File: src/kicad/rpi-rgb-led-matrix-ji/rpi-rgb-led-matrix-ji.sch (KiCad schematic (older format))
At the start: 41 parts, among them J1 Conn_01x02_Male, J2 Conn_02x10_Odd_Even, J3 Screw_Terminal_01x02, J4 Conn_02x08_Odd_Even, J5 Conn_02x08_Odd_Even, J6 Conn_02x08_Odd_Even, P1 Raspberry_Pi_2_3, Q1 DMG2305UX, Q2 DMMT5401, U1 74HCT245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

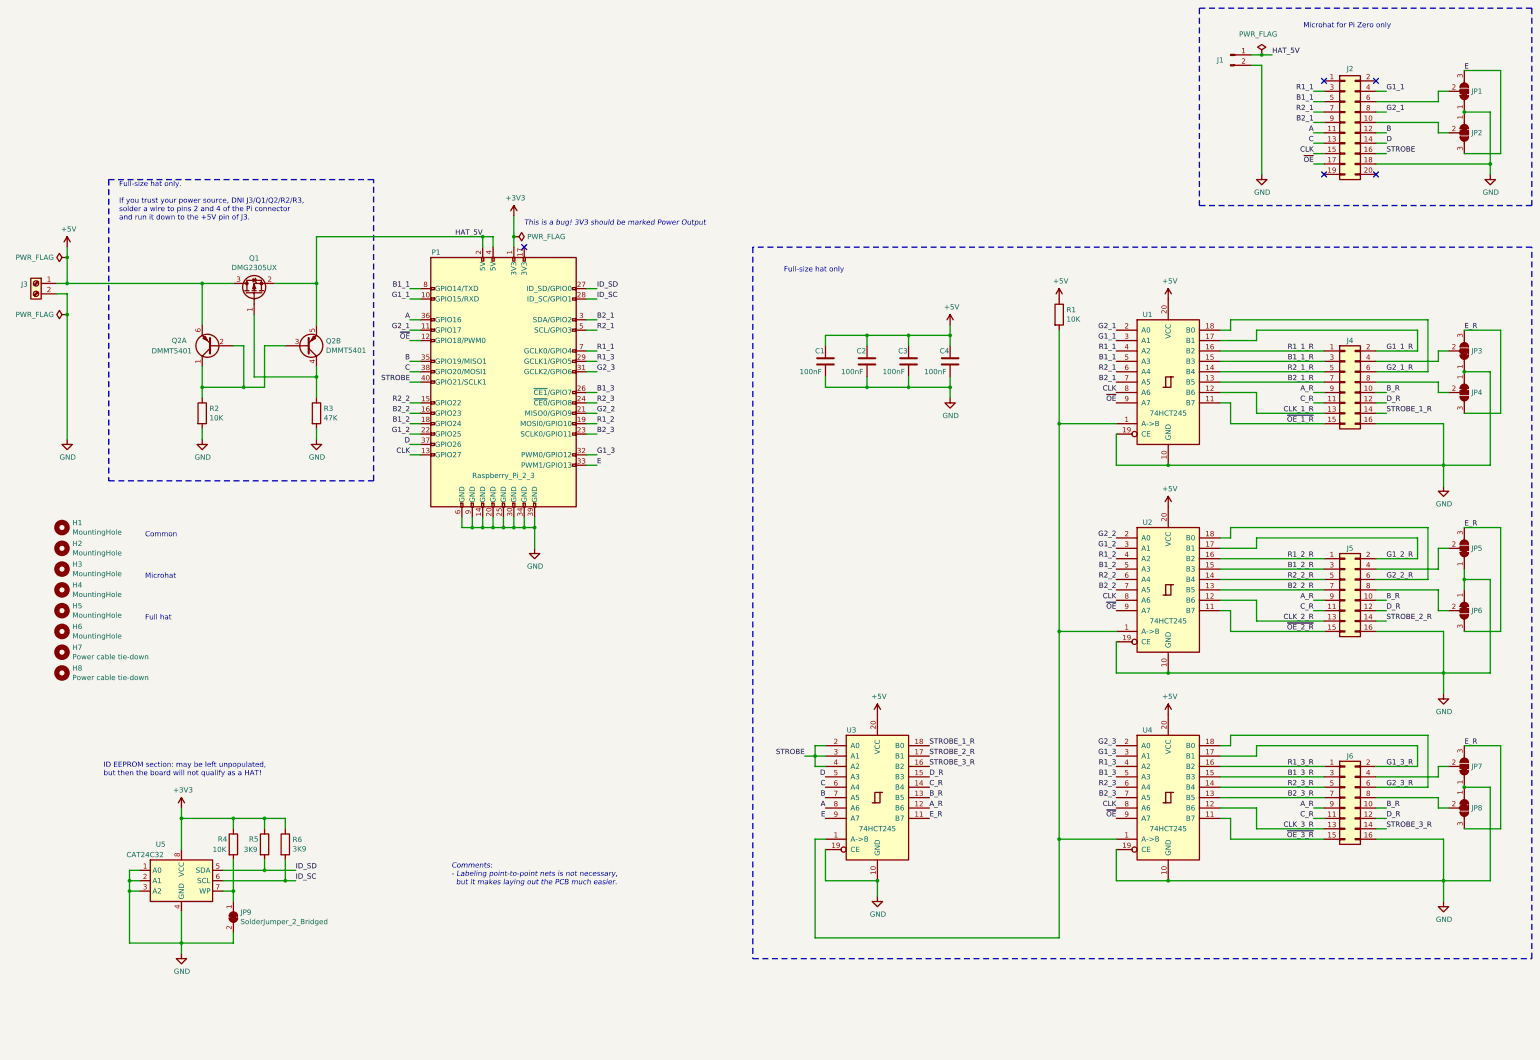
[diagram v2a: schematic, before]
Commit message: cleaned up PSU circuitry; added bypass capacitor to EEPROM
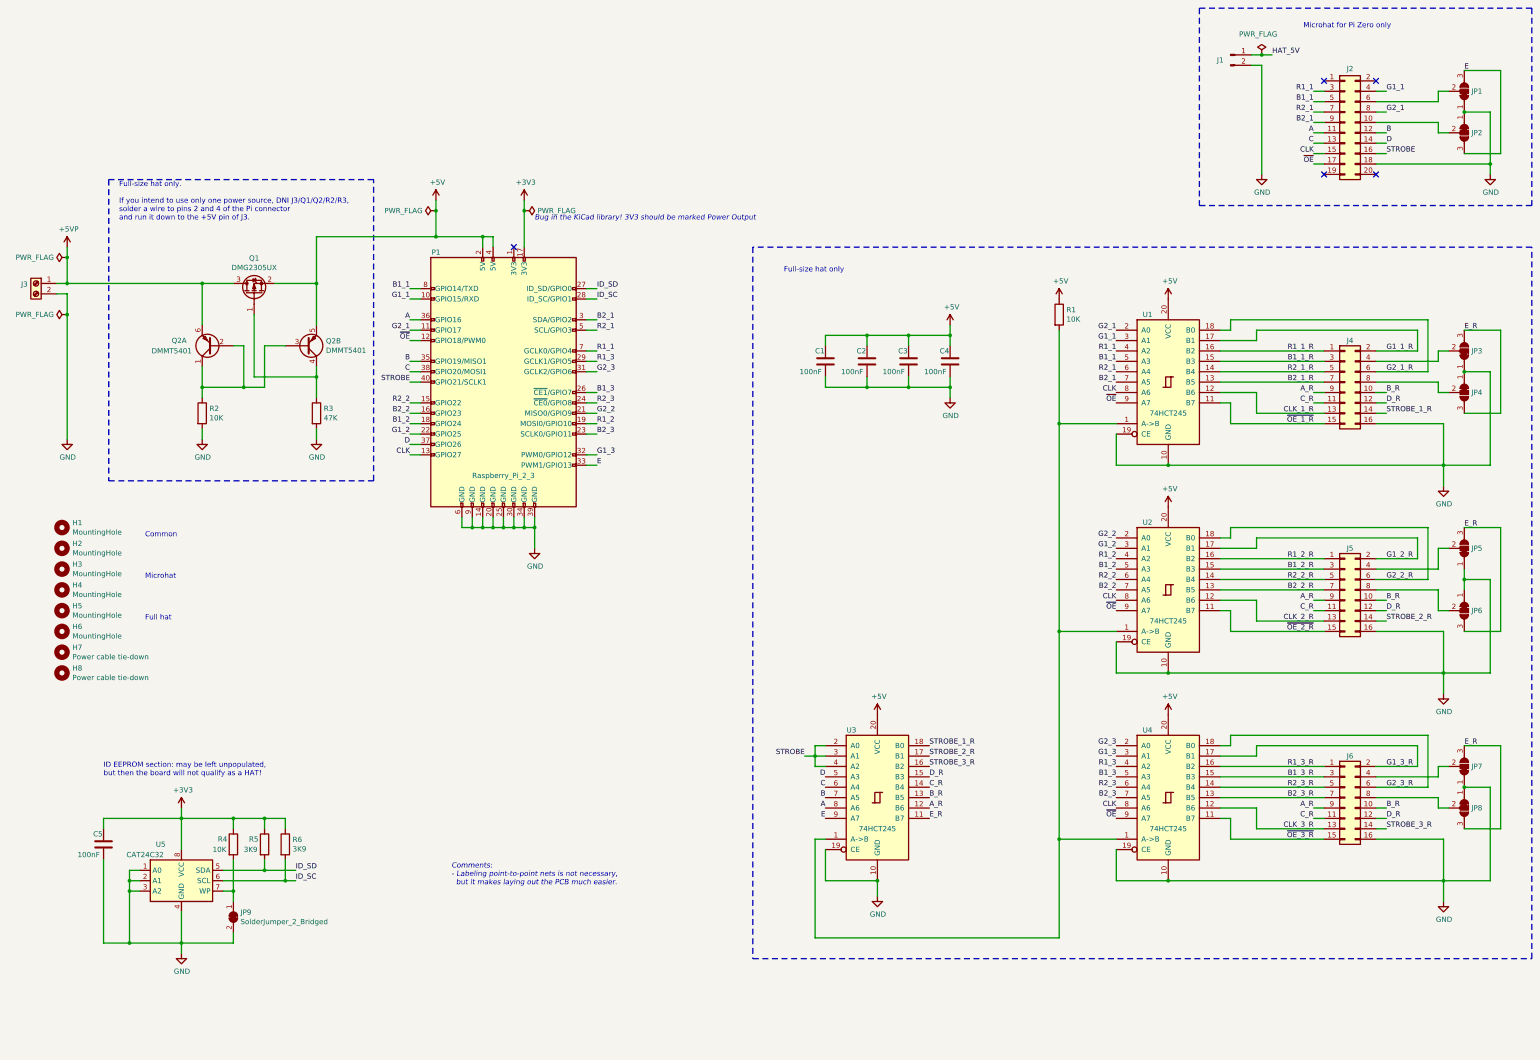
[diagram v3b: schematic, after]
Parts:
- added C5: 100nF, Capacitor_SMD:C_1206_3216Metric_Pad1.42x1.75mm_HandSolder, symbol Device:C
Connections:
- net +3V3: now also P1.17 (3V3), C5.1; no longer P1.1 (3V3)
- net +5V: now also P1.2 (5V), P1.4 (5V), Q1.2 (S), Q2.5 (E); no longer J3.1 (Pin_1), Q1.3 (D), Q2.6 (E)
- net GND: now also C5.2
- net HAT_5V: no longer P1.2 (5V), P1.4 (5V), Q1.2 (S), Q2.5 (E)
- new net +5VP: J3.1 (Pin_1), Q1.3 (D), Q2.6 (E)
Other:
- note added: "Bug in the KiCad library! 3V3 should be marked Power Output"
- note added: "Full-size hat only.\n\nIf you intend to use only one power source, DNI J3/Q1/Q2/R2/R3,\nsolder a wire to pins 2 and 4 of the Pi connector\nand run it down to the +5V pin of J3."
- note removed: "Full-size hat only.\n\nIf you trust your power source, DNI J3/Q1/Q2/R2/R3,\nsolder a wire to pins 2 and 4 of the Pi connector\nand run it down to the +5V pin of J3."
- note removed: "This is a bug! 3V3 should be marked Power Output"
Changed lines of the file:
@@
 Sheet 1 1
 Title "Led matrix driver"
-Date "2019-03-24"
-Rev "1.2.3"
+Date "2019-03-27"
+Rev "1.2.4"
 Comp "TLA CONSULTING, LLC"
 Comment1 ""
@@
 	0    -1   -1   0
 $EndComp
-NoConn ~ 5650 3050
 Wire Wire Line
 	13850 1550 13950 1550
@@
 L power:+3V3 #PWR03
 U 1 1 5CFC3CD8
-P 5550 2750
-F 0 "#PWR03" H 5550 2600 50  0001 C CNN
-F 1 "+3V3" H 5565 2923 50  0000 C CNN
-F 2 "" H 5550 2750 50  0001 C CNN
-F 3 "" H 5550 2750 50  0001 C CNN
-	1    5550 2750
-	1    0    0    -1
-$EndComp
-Wire Wire Line
-	5550 3050 5550 2950
+P 5650 2600
+F 0 "#PWR03" H 5650 2450 50  0001 C CNN
+F 1 "+3V3" H 5665 2773 50  0000 C CNN
+F 2 "" H 5650 2600 50  0001 C CNN
+F 3 "" H 5650 2600 50  0001 C CNN
+	1    5650 2600
+	1    0    0    -1
+$EndComp
 Wire Wire Line
 	2350 8450 2350 8550
@@
 L power:PWR_FLAG #FLG02
 U 1 1 5D3BB982
-P 5550 2950
-F 0 "#FLG02" H 5550 3025 50  0001 C CNN
-F 1 "PWR_FLAG" V 5550 3078 50  0000 L CNN
-F 2 "" H 5550 2950 50  0001 C CNN
-F 3 "~" H 5550 2950 50  0001 C CNN
-	1    5550 2950
+P 5650 2700
+F 0 "#FLG02" H 5650 2775 50  0001 C CNN
+F 1 "PWR_FLAG" V 5650 2828 50  0000 L CNN
+F 2 "" H 5650 2700 50  0001 C CNN
+F 3 "~" H 5650 2700 50  0001 C CNN
+	1    5650 2700
 	0    1    -1   0
 $EndComp
-Connection ~ 5550 2950
-Wire Wire Line
-	5550 2950 5550 2750
-Text Notes 5650 2850 0    50   Italic 0
-This is a bug! 3V3 should be marked Power Output
+Text Notes 5750 2800 0    50   Italic 0
+Bug in the KiCad library! 3V3 should be marked Power Output
 Wire Wire Line
 	3650 3800 3650 3400
@@
 	3650 3400 3650 2950
 Connection ~ 3650 3400
-$Comp
-L power:+5V #PWR04
-U 1 1 5D3FF8A0
-P 1250 3050
-F 0 "#PWR04" H 1250 2900 50  0001 C CNN
-F 1 "+5V" H 1265 3223 50  0000 C CNN
-F 2 "" H 1250 3050 50  0001 C CNN
-F 3 "" H 1250 3050 50  0001 C CNN
-	1    1250 3050
-	1    0    0    -1
-$EndComp
-Wire Wire Line
-	1250 3050 1250 3150
+Wire Wire Line
+	4800 2600 4800 2700
 $Comp
 L power:PWR_FLAG #FLG03
 U 1 1 5D42AE8D
-P 1250 3150
-F 0 "#FLG03" H 1250 3225 50  0001 C CNN
-F 1 "PWR_FLAG" V 1250 3278 50  0000 L CNN
-F 2 "" H 1250 3150 50  0001 C CNN
-F 3 "~" H 1250 3150 50  0001 C CNN
-	1    1250 3150
+P 4800 2700
+F 0 "#FLG03" H 4800 2775 50  0001 C CNN
+F 1 "PWR_FLAG" V 4800 2828 50  0000 L CNN
+F 2 "" H 4800 2700 50  0001 C CNN
+F 3 "~" H 4800 2700 50  0001 C CNN
+	1    4800 2700
 	0    -1   -1   0
 $EndComp
-Connection ~ 1250 3150
-Wire Wire Line
-	1250 3150 1250 3400
+Connection ~ 4800 2700
+Wire Wire Line
+	4800 2700 4800 2950
 $Comp
 L power:PWR_FLAG #FLG01
@@
 Wire Wire Line
 	1150 3500 1250 3500
-Wire Wire Line
-	1150 3400 1250 3400
 Connection ~ 1250 3700
 Wire Wire Line
@@
 	1    0    0    -1
 $EndComp
-Text Label 5250 2950 2    50   ~ 0
-HAT_5V
 Wire Notes Line
 	12150 750  15350 750
@@
 ID EEPROM section: may be left unpopulated,\nbut then the board will not qualify as a HAT!
 Wire Wire Line
-	3650 2950 5250 2950
+	3650 2950 4800 2950
 Connection ~ 5250 2950
-Connection ~ 1250 3400
 Connection ~ 2550 3400
 Wire Wire Line
@@
 	1650 2400 1650 5300
 Text Notes 1750 2800 0    50   ~ 0
-Full-size hat only.\n\nIf you trust your power source, DNI J3/Q1/Q2/R2/R3,\nsolder a wire to pins 2 and 4 of the Pi connector\nand run it down to the +5V pin of J3.
+Full-size hat only.\n\nIf you intend to use only one power source, DNI J3/Q1/Q2/R2/R3,\nsolder a wire to pins 2 and 4 of the Pi connector\nand run it down to the +5V pin of J3.
+$Comp
+L Device:C C5
+U 1 1 5CAEBB5A
+P 1600 8800
+F 0 "C5" H 1500 8900 50  0000 L CNN
+F 1 "100nF" H 1350 8700 50  0000 L CNN
+F 2 "Capacitor_SMD:C_1206_3216Metric_Pad1.42x1.75mm_HandSolder" H 1638 8650 50  0001 C CNN
+F 3 "https://katalog.we-online.de/pbs/datasheet/885012208087.pdf" H 1600 8800 50  0001 C CNN
+F 4 "732-8127-1-ND" H -8150 4650 50  0001 C CNN "DigiKey part number"
+F 5 "885012208087" H -8150 4650 50  0001 C CNN "Mfg part number"
+	1    1600 8800
+	1    0    0    -1
+$EndComp
+Wire Wire Line
+	1600 8550 1600 8650
+Connection ~ 4800 2950
+Wire Wire Line
+	4800 2950 5250 2950
+Wire Wire Line
+	1150 3400 1250 3400
+Wire Wire Line
+	5650 2600 5650 2700
+Connection ~ 5650 2700
+Wire Wire Line
+	5650 2700 5650 3050
+NoConn ~ 5550 3050
+Wire Wire Line
+	1250 3050 1250 3150
+$Comp
+L power:PWR_FLAG #FLG0101
+U 1 1 5CBFC03E
+P 1250 3150
+F 0 "#FLG0101" H 1250 3225 50  0001 C CNN
+F 1 "PWR_FLAG" V 1250 3278 50  0000 L CNN
+F 2 "" H 1250 3150 50  0001 C CNN
+F 3 "~" H 1250 3150 50  0001 C CNN
+	1    1250 3150
+	0    -1   -1   0
+$EndComp
+Connection ~ 1250 3150
+Wire Wire Line
+	1250 3150 1250 3400
+Connection ~ 1250 3400
 Wire Wire Line
 	1250 3400 2550 3400
+$Comp
+L power:+5V #PWR04
+U 1 1 5D3FF8A0
+P 4800 2600
+F 0 "#PWR04" H 4800 2450 50  0001 C CNN
+F 1 "+5V" H 4815 2773 50  0000 C CNN
+F 2 "" H 4800 2600 50  0001 C CNN
+F 3 "" H 4800 2600 50  0001 C CNN
+	1    4800 2600
+	1    0    0    -1
+$EndComp
+$Comp
+L power:+5VP #PWR0101
+U 1 1 5CC6ABBE
+P 1250 3050
+F 0 "#PWR0101" H 1250 2900 50  0001 C CNN
+F 1 "+5VP" H 1265 3223 50  0000 C CNN
+F 2 "" H 1250 3050 50  0001 C CNN
+F 3 "" H 1250 3050 50  0001 C CNN
+	1    1250 3050
+	1    0    0    -1
+$EndComp
+Wire Wire Line
+	1600 8550 2350 8550
+Wire Wire Line
+	1600 9750 1850 9750
+Wire Wire Line
+	1600 8950 1600 9750
+Connection ~ 1850 9750
 $EndSCHEMATC
